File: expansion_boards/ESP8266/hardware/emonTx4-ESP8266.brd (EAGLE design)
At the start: 51 x 31 mm, 13 parts, among them IC1 2471

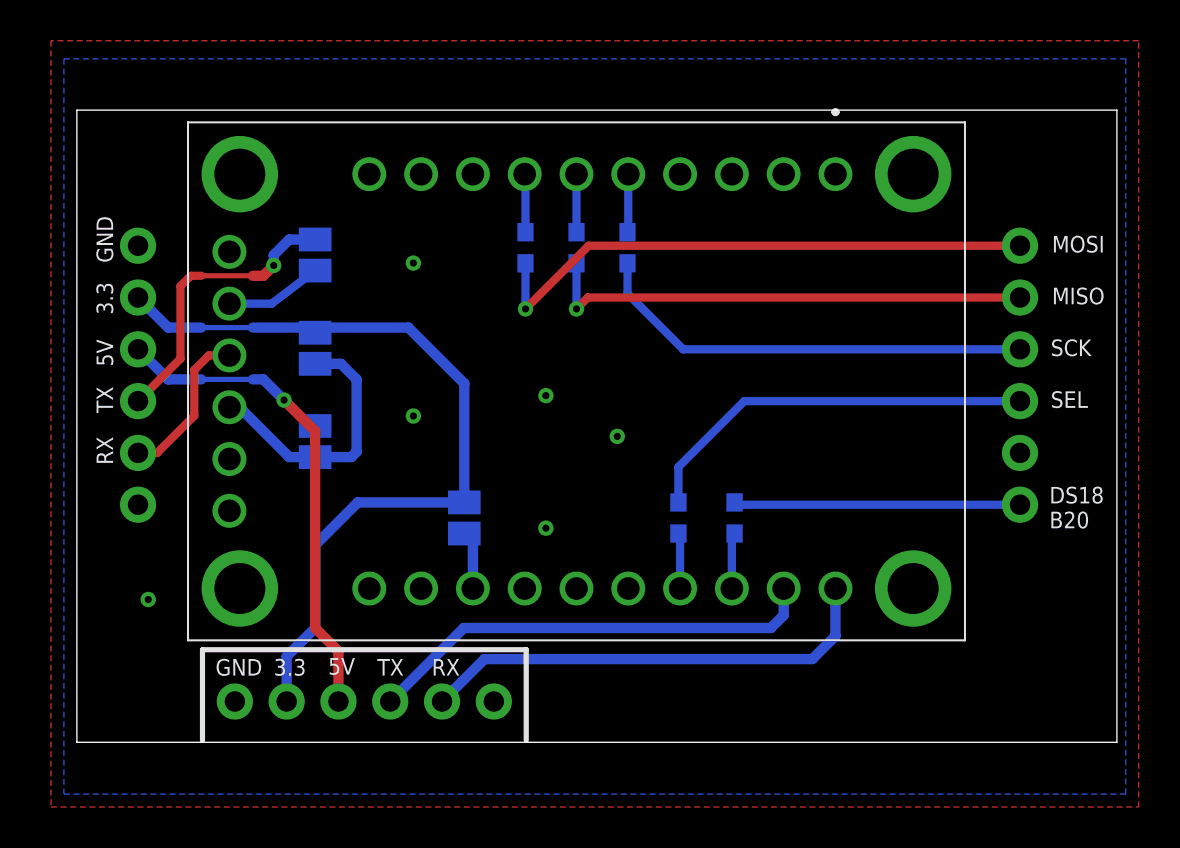
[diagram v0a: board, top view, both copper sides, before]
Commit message: updated ESP8266 adapter board
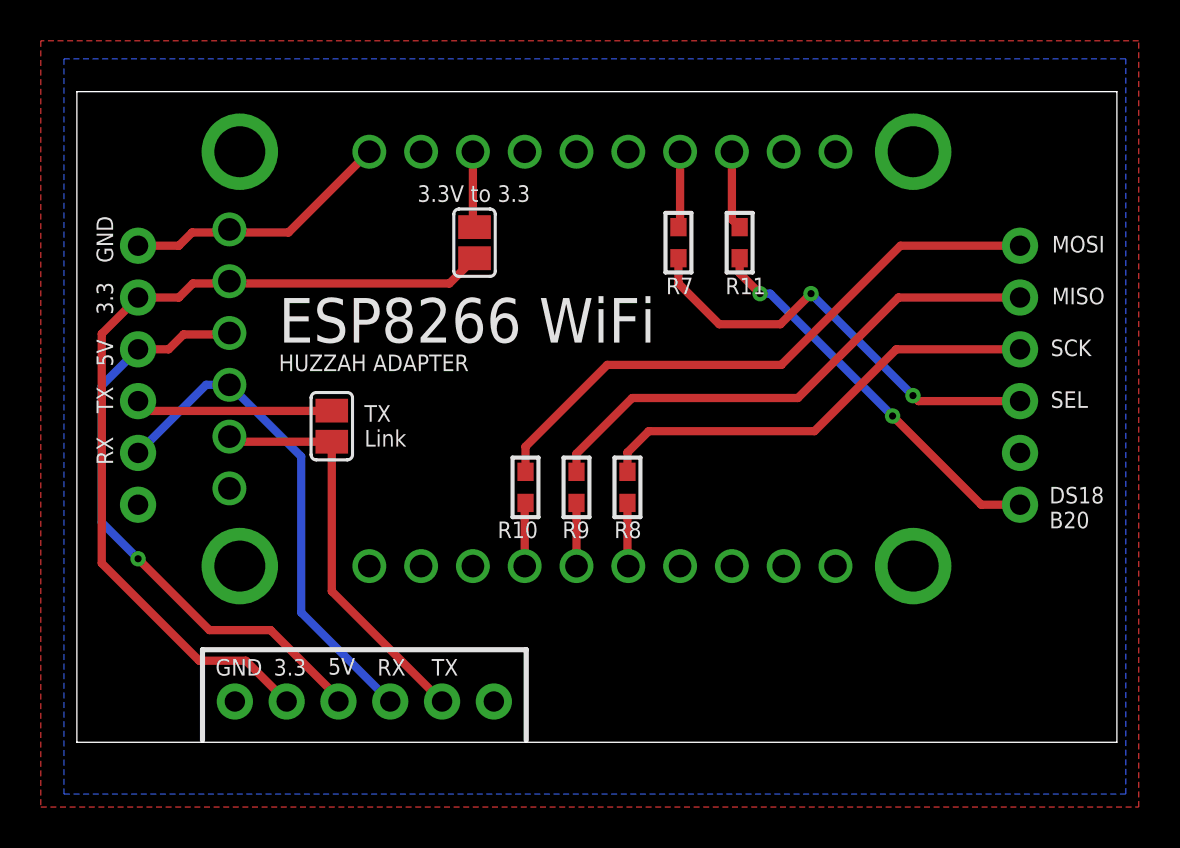
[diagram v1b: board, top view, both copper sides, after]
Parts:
- removed SJ1, SJ2: (no value), jumper:SJ
- moved SJ3 13.5 mm to (19.5, 25.5), flipped to the top, turned to 90 degrees
- moved R11 13.5 mm to (32.5, 25.5), flipped to the top, turned to 90 degrees
- moved R7 13.5 mm to (29.5, 25.5), flipped to the top, turned to 90 degrees
- moved R10 11.8 mm to (22.0, 13.5), flipped to the top, turned to 90 degrees
- moved R8 11.8 mm to (27.0, 13.5), flipped to the top, turned to 90 degrees
- moved R9 11.8 mm to (24.5, 13.5), flipped to the top, turned to 90 degrees
- moved SJ4 8.43 mm to (12.5, 16.5), flipped to the top
- moved IC1 0.50 mm to (24.5, 19.5), flipped to the bottom, turned to 180 degrees
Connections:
- removed net N$6: IC1.24, SJ1.1, SJ2.1
- net 3.3V: now also IC1.25; no longer SJ1.2
- net 5V: now also IC1.24; no longer SJ2.2
- net ESP_RX: now also JP3.3
- net ESP_RX1: no longer JP3.3
- net ESP_TX: now also JP3.2
- net ESP_TX1: no longer JP3.2
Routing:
- net ESP_TX1: track 23.0 -> 0.00 mm
- net ESP_RX1: track 22.4 -> 0.00 mm
- net ESP_RX: track 7.82 -> 24.7 mm
- net ESP_TX: track 4.75 -> 20.1 mm
- net GND: track 0.00 -> 13.4 mm, vias 6 -> 0
- net N$6: track 13.3 -> 0.00 mm
- net N$1: track 15.0 -> 9.70 mm, vias 1 -> 0
- net DS18B20: track 14.0 -> 19.2 mm, vias 0 -> 2
- net 5V: track 26.1 -> 29.4 mm
- net 3.3V: track 40.2 -> 43.0 mm
- net RFM_SEL: track 19.8 -> 21.6 mm, vias 0 -> 2
- net RFM_MOSI: track 27.8 -> 29.6 mm, vias 1 -> 0
- net RFM_MISO: track 24.2 -> 25.8 mm, vias 1 -> 0
- net N$9: track 2.86 -> 4.02 mm
- net N$12: track 2.75 -> 3.86 mm
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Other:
- board size 51 x 31 mm -> 51 x 31.9 mm
- board text added: "ESP8266 WiFi"
- board text added: "HUZZAH ADAPTER"
- board text removed: "3.3V to Vin"
- board text removed: "5V to Vin"
